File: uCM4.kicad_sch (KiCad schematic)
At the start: 30 parts, among them J1 Conn_01x03, J2 Ethernet, J3 Micro_SD_Card, J4 USB_B_Micro, SW1 SW_DIP_x01, SW2 SW_DIP_x01, U1 RT9742GGJ5, U2 74LVC1G07, U3 TPD4EUSB30

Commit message: Power rail again
Hopefully the last time.
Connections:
- net nPWR_LED: now reaches Module1.95 (nPI_LED_PWR), U2.2
- net nPWR_LED_Buffered: now reaches R13.1, U2.4
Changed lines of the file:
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@@
   (junction (at 137.16 68.58) (diameter 1.016) (color 0 0 0 0))
   (junction (at 146.05 152.4) (diameter 1.016) (color 0 0 0 0))
+  (junction (at 148.59 157.48) (diameter 1.016) (color 0 0 0 0))
+  (junction (at 148.59 194.31) (diameter 1.016) (color 0 0 0 0))
   (junction (at 164.465 38.1) (diameter 1.016) (color 0 0 0 0))
   (junction (at 165.1 58.42) (diameter 1.016) (color 0 0 0 0))
@@
     (stroke (width 0) (type solid) (color 0 0 0 0))
   )
+  (wire (pts (xy 140.335 194.31) (xy 148.59 194.31))
+    (stroke (width 0) (type solid) (color 0 0 0 0))
+  )
   (wire (pts (xy 140.97 166.37) (xy 144.78 166.37))
     (stroke (width 0) (type solid) (color 0 0 0 0))
@@
   )
   (wire (pts (xy 148.59 157.48) (xy 148.59 175.26))
+    (stroke (width 0) (type solid) (color 0 0 0 0))
+  )
+  (wire (pts (xy 148.59 157.48) (xy 159.385 157.48))
     (stroke (width 0) (type solid) (color 0 0 0 0))
   )
@@
     (effects (font (size 1.27 1.27)) (justify left bottom))
   )
+  (label "nPWR_LED_Buffered" (at 140.335 194.31 180)
+    (effects (font (size 1.27 1.27)) (justify right bottom))
+  )
   (label "SD_PWR" (at 146.05 155.575 0)
     (effects (font (size 1.27 1.27)) (justify left bottom))
   )
+  (label "nPWR_LED" (at 159.385 157.48 0)
+    (effects (font (size 1.27 1.27)) (justify left bottom))
+  )

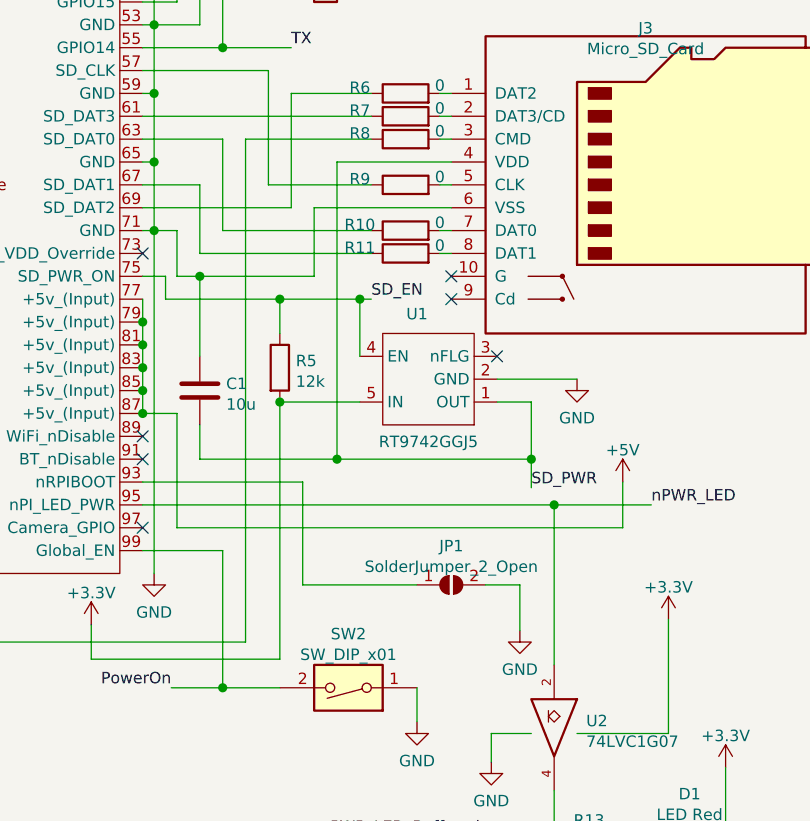
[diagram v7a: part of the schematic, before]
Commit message: Fix Micro SD connector
Most likely is generally fine now. Some rerouting was required due to
the change in footprint layout.
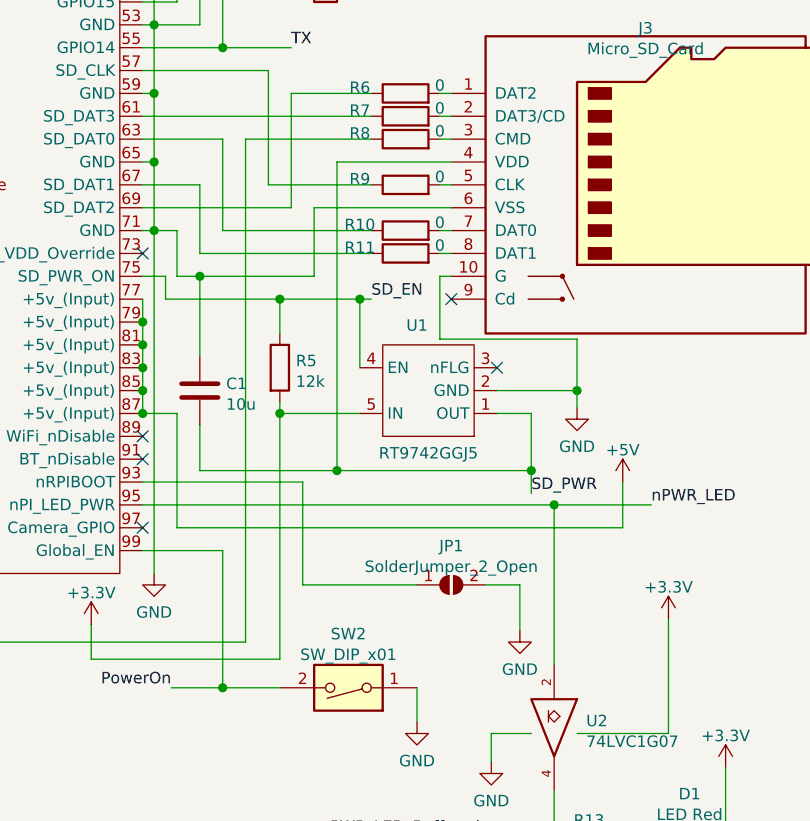
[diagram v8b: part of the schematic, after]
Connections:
- net GND: now also J3.10 (G)
- no-connect marks 113 -> 112
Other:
- moved on the sheet: U1
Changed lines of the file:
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@@
   (junction (at 111.76 177.8) (diameter 1.016) (color 0 0 0 0))
   (junction (at 118.11 134.62) (diameter 1.016) (color 0 0 0 0))
-  (junction (at 118.11 146.05) (diameter 1.016) (color 0 0 0 0))
+  (junction (at 118.11 147.32) (diameter 1.016) (color 0 0 0 0))
   (junction (at 122.555 58.42) (diameter 1.016) (color 0 0 0 0))
-  (junction (at 124.46 152.4) (diameter 1.016) (color 0 0 0 0))
+  (junction (at 124.46 153.67) (diameter 1.016) (color 0 0 0 0))
   (junction (at 126.365 53.34) (diameter 1.016) (color 0 0 0 0))
   (junction (at 127 41.275) (diameter 1.016) (color 0 0 0 0))
@@
   (junction (at 128.905 38.1) (diameter 1.016) (color 0 0 0 0))
   (junction (at 137.16 68.58) (diameter 1.016) (color 0 0 0 0))
-  (junction (at 146.05 152.4) (diameter 1.016) (color 0 0 0 0))
+  (junction (at 146.05 153.67) (diameter 1.016) (color 0 0 0 0))
   (junction (at 148.59 157.48) (diameter 1.016) (color 0 0 0 0))
   (junction (at 148.59 194.31) (diameter 1.016) (color 0 0 0 0))
+  (junction (at 151.13 144.78) (diameter 1.016) (color 0 0 0 0))
   (junction (at 164.465 38.1) (diameter 1.016) (color 0 0 0 0))
   (junction (at 165.1 58.42) (diameter 1.016) (color 0 0 0 0))
@@
   (no_connect (at 102.87 152.4))
   (no_connect (at 102.87 160.02))
-  (no_connect (at 137.16 132.08))
   (no_connect (at 137.16 134.62))
-  (no_connect (at 142.24 140.97))
+  (no_connect (at 142.24 142.24))
   (no_connect (at 187.96 36.83))
   (no_connect (at 187.96 39.37))
@@
     (stroke (width 0) (type solid) (color 0 0 0 0))
   )
-  (wire (pts (xy 109.22 148.59) (xy 109.22 152.4))
-    (stroke (width 0) (type solid) (color 0 0 0 0))
-  )
-  (wire (pts (xy 109.22 152.4) (xy 124.46 152.4))
+  (wire (pts (xy 109.22 148.59) (xy 109.22 153.67))
+    (stroke (width 0) (type solid) (color 0 0 0 0))
+  )
+  (wire (pts (xy 109.22 153.67) (xy 124.46 153.67))
     (stroke (width 0) (type solid) (color 0 0 0 0))
   )
@@
     (stroke (width 0) (type solid) (color 0 0 0 0))
   )
-  (wire (pts (xy 118.11 146.05) (xy 127 146.05))
-    (stroke (width 0) (type solid) (color 0 0 0 0))
-  )
-  (wire (pts (xy 118.11 174.625) (xy 118.11 146.05))
+  (wire (pts (xy 118.11 147.32) (xy 118.11 146.05))
+    (stroke (width 0) (type solid) (color 0 0 0 0))
+  )
+  (wire (pts (xy 118.11 147.32) (xy 127 147.32))
+    (stroke (width 0) (type solid) (color 0 0 0 0))
+  )
+  (wire (pts (xy 118.11 174.625) (xy 118.11 147.32))
     (stroke (width 0) (type solid) (color 0 0 0 0))
   )
@@
     (stroke (width 0) (type solid) (color 0 0 0 0))
   )
-  (wire (pts (xy 124.46 119.38) (xy 124.46 152.4))
+  (wire (pts (xy 124.46 119.38) (xy 124.46 153.67))
     (stroke (width 0) (type solid) (color 0 0 0 0))
   )
@@
     (stroke (width 0) (type solid) (color 0 0 0 0))
   )
-  (wire (pts (xy 124.46 152.4) (xy 146.05 152.4))
+  (wire (pts (xy 124.46 153.67) (xy 146.05 153.67))
     (stroke (width 0) (type solid) (color 0 0 0 0))
   )
@@
     (stroke (width 0) (type solid) (color 0 0 0 0))
   )
-  (wire (pts (xy 127 134.62) (xy 127 140.97))
+  (wire (pts (xy 127 134.62) (xy 127 142.24))
     (stroke (width 0) (type solid) (color 0 0 0 0))
   )
@@
     (stroke (width 0) (type solid) (color 0 0 0 0))
   )
+  (wire (pts (xy 135.89 132.08) (xy 135.89 139.065))
+    (stroke (width 0) (type solid) (color 0 0 0 0))
+  )
+  (wire (pts (xy 135.89 139.065) (xy 151.13 139.065))
+    (stroke (width 0) (type solid) (color 0 0 0 0))
+  )
   (wire (pts (xy 137.16 66.04) (xy 137.16 68.58))
     (stroke (width 0) (type solid) (color 0 0 0 0))
@@
     (stroke (width 0) (type solid) (color 0 0 0 0))
   )
+  (wire (pts (xy 137.16 132.08) (xy 135.89 132.08))
+    (stroke (width 0) (type solid) (color 0 0 0 0))
+  )
   (wire (pts (xy 140.335 194.31) (xy 148.59 194.31))
     (stroke (width 0) (type solid) (color 0 0 0 0))
@@
     (stroke (width 0) (type solid) (color 0 0 0 0))
   )
-  (wire (pts (xy 142.24 143.51) (xy 151.13 143.51))
+  (wire (pts (xy 142.24 144.78) (xy 151.13 144.78))
+    (stroke (width 0) (type solid) (color 0 0 0 0))
+  )
+  (wire (pts (xy 142.24 147.32) (xy 146.05 147.32))
     (stroke (width 0) (type solid) (color 0 0 0 0))
   )
@@
     (stroke (width 0) (type solid) (color 0 0 0 0))
   )
-  (wire (pts (xy 146.05 146.05) (xy 142.24 146.05))
-    (stroke (width 0) (type solid) (color 0 0 0 0))
-  )
-  (wire (pts (xy 146.05 146.05) (xy 146.05 152.4))
-    (stroke (width 0) (type solid) (color 0 0 0 0))
-  )
-  (wire (pts (xy 146.05 155.575) (xy 146.05 152.4))
+  (wire (pts (xy 146.05 147.32) (xy 146.05 153.67))
+    (stroke (width 0) (type solid) (color 0 0 0 0))
+  )
+  (wire (pts (xy 146.05 153.67) (xy 146.05 156.21))
     (stroke (width 0) (type solid) (color 0 0 0 0))
   )
@@
   )
   (wire (pts (xy 151.13 22.86) (xy 151.13 24.765))
+    (stroke (width 0) (type solid) (color 0 0 0 0))
+  )
+  (wire (pts (xy 151.13 139.065) (xy 151.13 144.78))
+    (stroke (width 0) (type solid) (color 0 0 0 0))
+  )
+  (wire (pts (xy 151.13 144.78) (xy 151.13 146.685))
     (stroke (width 0) (type solid) (color 0 0 0 0))
   )
@@
     (effects (font (size 1.27 1.27)) (justify right bottom))
   )
-  (label "SD_PWR" (at 146.05 155.575 0)
+  (label "SD_PWR" (at 146.05 156.21 0)
     (effects (font (size 1.27 1.27)) (justify left bottom))
   )
@@
     (pin "1")
   )
-  (symbol (lib_id "power:GND") (at 151.13 143.51 0) (unit 1)
-    (in_bom yes) (on_board yes)
-    (property "Reference" "#PWR0112" (id 0) (at 151.13 149.86 0)
-      (effects (font (size 1.27 1.27)) hide)
-    )
-    (property "Value" "GND" (id 1) (at 151.13 147.8344 0))
-    (property "Footprint" "" (id 2) (at 151.13 143.51 0)
-      (effects (font (size 1.27 1.27)) hide)
-    )
-    (property "Datasheet" "" (id 3) (at 151.13 143.51 0)
+  (symbol (lib_id "power:GND") (at 151.13 146.685 0) (unit 1)
+    (in_bom yes) (on_board yes)
+    (property "Reference" "#PWR0112" (id 0) (at 151.13 153.035 0)
+      (effects (font (size 1.27 1.27)) hide)
+    )
+    (property "Value" "GND" (id 1) (at 151.13 151.0094 0))
+    (property "Footprint" "" (id 2) (at 151.13 146.685 0)
+      (effects (font (size 1.27 1.27)) hide)
+    )
+    (property "Datasheet" "" (id 3) (at 151.13 146.685 0)
       (effects (font (size 1.27 1.27)) hide)
     )
@@
     (pin "5")
   )
-  (symbol (lib_id "CM4IO:RT9742GGJ5") (at 133.35 135.89 180) (unit 1)
-    (in_bom yes) (on_board yes)
-    (property "Reference" "U1" (id 0) (at 133.35 136.271 0))
-    (property "Value" "RT9742GGJ5" (id 1) (at 134.62 150.4696 0))
-    (property "Footprint" "Package_TO_SOT_SMD:SOT-23-5" (id 2) (at 133.35 135.89 0)
-      (effects (font (size 1.27 1.27)) hide)
-    )
-    (property "Datasheet" "https://www.richtek.com/assets/product_file/RT9742/DS9742-00.pdf" (id 3) (at 133.35 135.89 0)
-      (effects (font (size 1.27 1.27)) hide)
-    )
-    (property "Field4" "Farnell" (id 4) (at 133.35 135.89 0)
-      (effects (font (size 1.27 1.27)) hide)
-    )
-    (property "Field5" "	2545875" (id 5) (at 133.35 135.89 0)
-      (effects (font (size 1.27 1.27)) hide)
-    )
-    (property "Field6" "RT9742GGJ5" (id 6) (at 133.35 135.89 0)
-      (effects (font (size 1.27 1.27)) hide)
-    )
-    (property "Field7" "RichTek" (id 7) (at 133.35 135.89 0)
-      (effects (font (size 1.27 1.27)) hide)
-    )
-    (property "Field8" "USWI00166" (id 8) (at 133.35 135.89 0)
-      (effects (font (size 1.27 1.27)) hide)
-    )
-    (property "Part Description" "	Power Switch/Driver 1:1 N-Channel 1A TSOT-23-5" (id 9) (at 133.35 135.89 0)
-      (effects (font (size 1.27 1.27)) hide)
-    )
+  (symbol (lib_id "CM4IO:RT9742GGJ5") (at 133.35 137.16 180) (unit 1)
+    (in_bom yes) (on_board yes)
+    (property "Reference" "U1" (id 0) (at 133.35 137.541 0))
+    (property "Value" "RT9742GGJ5" (id 1) (at 134.62 151.7396 0))
+    (property "Footprint" "Package_TO_SOT_SMD:SOT-23-5" (id 2) (at 133.35 137.16 0)
+      (effects (font (size 1.27 1.27)) hide)
+    )
+    (property "Datasheet" "https://www.richtek.com/assets/product_file/RT9742/DS9742-00.pdf" (id 3) (at 133.35 137.16 0)
+      (effects (font (size 1.27 1.27)) hide)
+    )
+    (property "Field4" "Farnell" (id 4) (at 133.35 137.16 0)
+      (effects (font (size 1.27 1.27)) hide)
+    )
+    (property "Field5" "	2545875" (id 5) (at 133.35 137.16 0)
+      (effects (font (size 1.27 1.27)) hide)
+    )
+    (property "Field6" "RT9742GGJ5" (id 6) (at 133.35 137.16 0)
+      (effects (font (size 1.27 1.27)) hide)
+    )
+    (property "Field7" "RichTek" (id 7) (at 133.35 137.16 0)
+      (effects (font (size 1.27 1.27)) hide)
+    )
+    (property "Field8" "USWI00166" (id 8) (at 133.35 137.16 0)
+      (effects (font (size 1.27 1.27)) hide)
+    )
+    (property "Part Description" "	Power Switch/Driver 1:1 N-Channel 1A TSOT-23-5" (id 9) (at 133.35 137.16 0)
+      (effects (font (size 1.27 1.27)) hide)
+    )
